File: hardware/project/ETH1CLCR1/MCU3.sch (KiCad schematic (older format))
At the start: 19 parts, among them J601 Conn_02x05, U601 STM32F413RGT6Tx, U602 24LC08B-E/MS, Y601 NX3225GD-8MHZ-STD-CRA-3

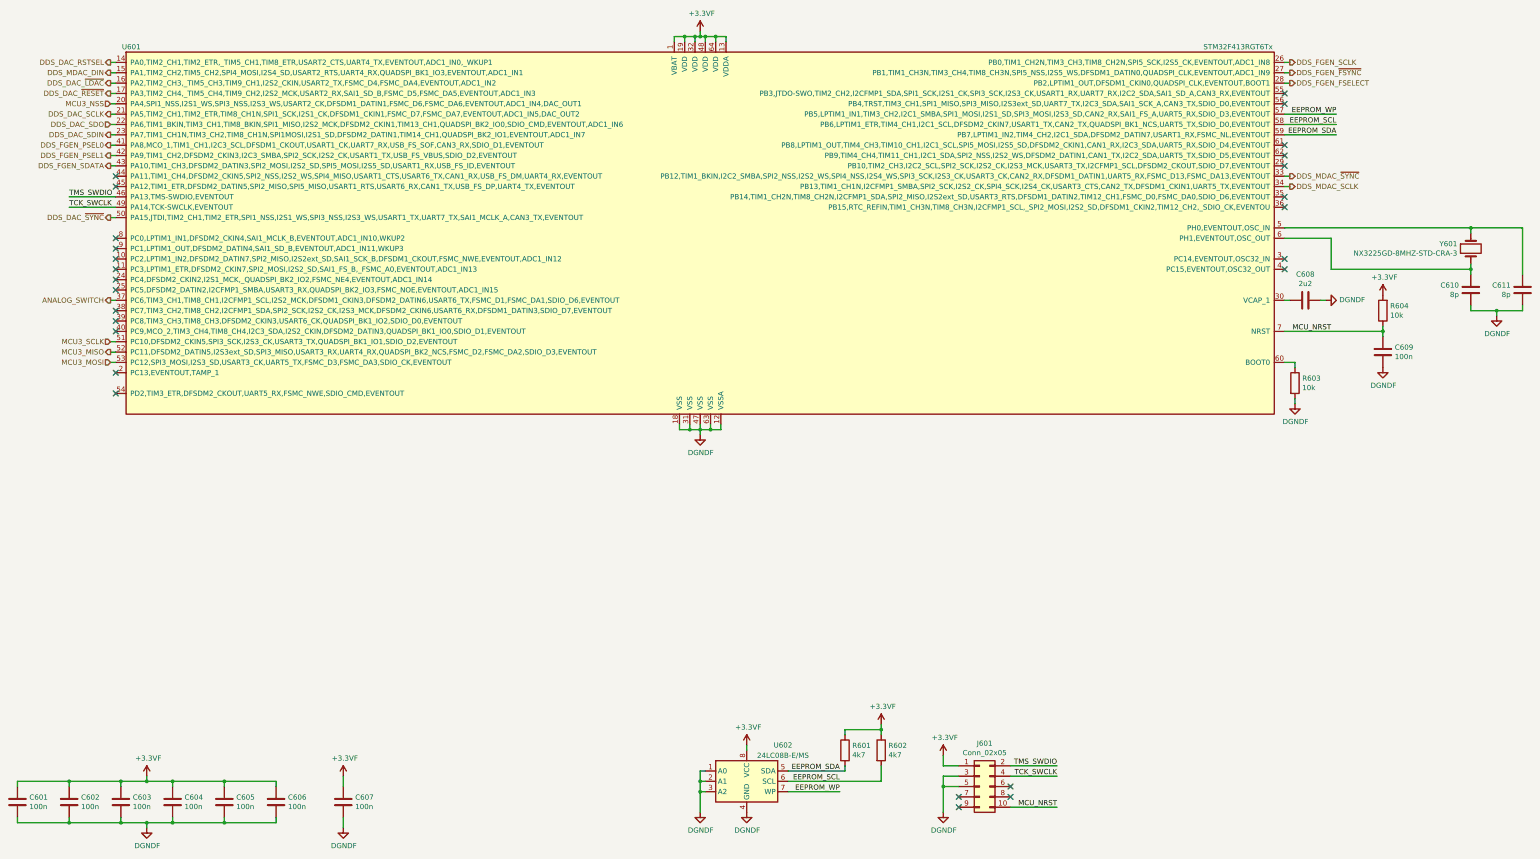
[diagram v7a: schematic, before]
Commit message: Checked the schematics. Created BOM.
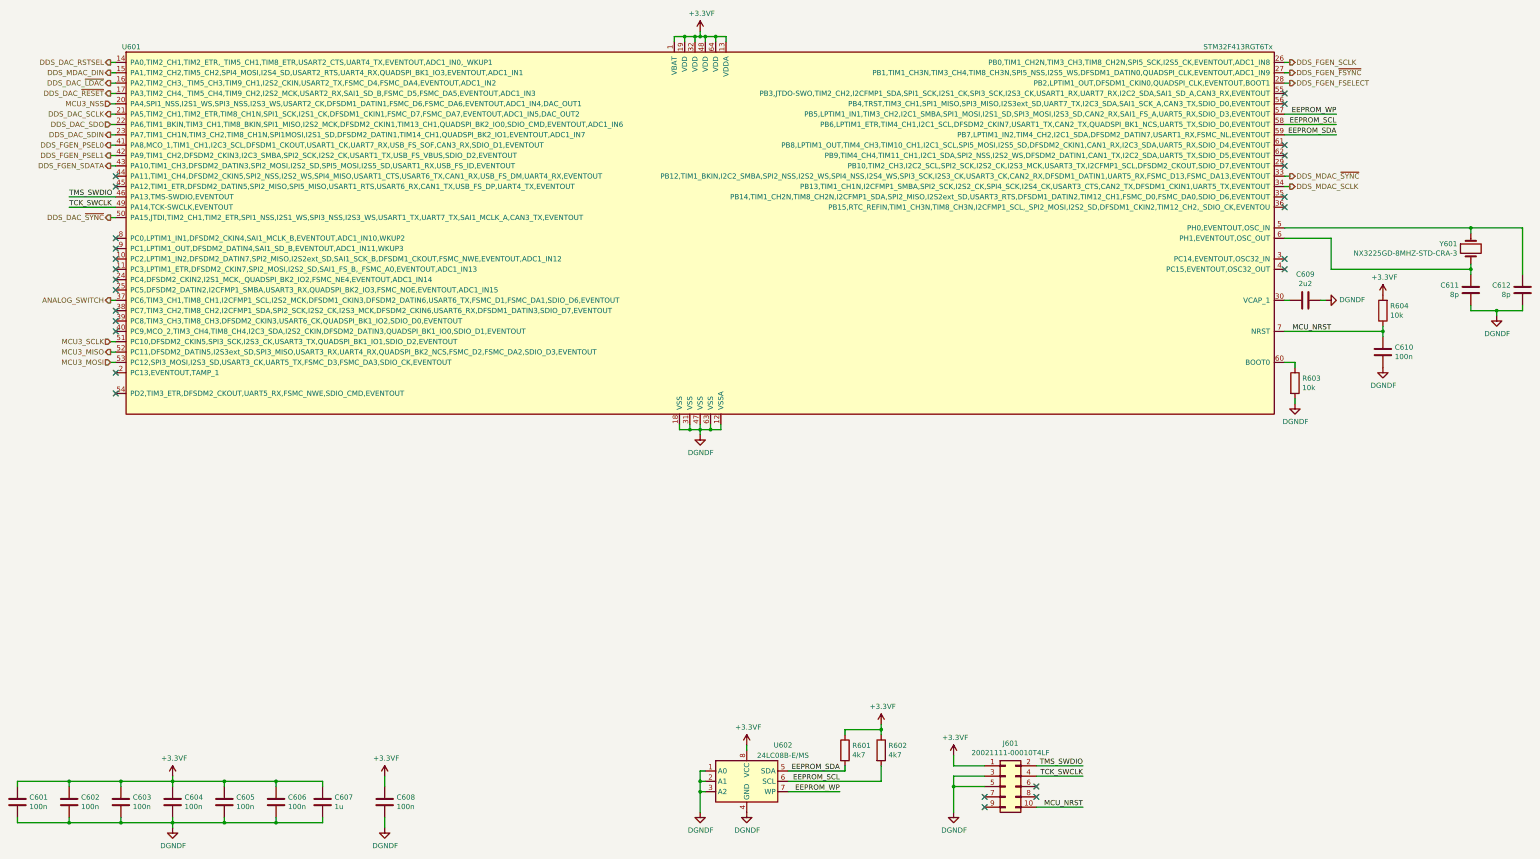
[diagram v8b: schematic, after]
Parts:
- added C607: 1u, Capacitor_SMD:C_0603_1608Metric_Pad1.05x0.95mm_HandSolder, symbol Device:C
- J601: value Conn_02x05 -> 20021111-00010T4LF
- renumbered C607 to C608, C608 to C609, C609 to C610, C610 to C611, C611 to C612
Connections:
- net +3.3VF: now also C607.1
- net DGNDF: now also C607.2
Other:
- moved on the sheet: C608, J601
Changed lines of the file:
@@
 encoding utf-8
 Sheet 6 15
-Title ""
-Date ""
-Rev ""
+Title "MCU3"
+Date "2020-01-19"
+Rev "1.0"
 Comp ""
-Comment1 ""
+Comment1 "Verification done."
 Comment2 ""
 Comment3 ""
@@
 L Connector_Generic:Conn_02x05_Odd_Even J?
 U 1 1 5E74C1A0
-P 10250 10350
+P 10500 10350
 AR Path="/5DCED281/5E74C1A0" Ref="J?"  Part="1"
 AR Path="/5DF35BC8/5E74C1A0" Ref="J?"  Part="1"
 AR Path="/5E29C232/5E74C1A0" Ref="J?"  Part="1"
 AR Path="/5DF38F82/5E74C1A0" Ref="J601"  Part="1"
-F 0 "J601" H 10300 10767 50  0000 C CNN
-F 1 "Conn_02x05" H 10300 10676 50  0000 C CNN
-F 2 "Connector_PinHeader_1.27mm:PinHeader_2x05_P1.27mm_Vertical" H 10250 10350 50  0001 C CNN
-F 3 "~" H 10250 10350 50  0001 C CNN
-	1    10250 10350
-	1    0    0    -1
-$EndComp
-NoConn ~ 10050 10450
-NoConn ~ 10050 10550
-Wire Wire Line
-	10050 10350 9900 10350
-Wire Wire Line
-	9900 10350 9900 10250
-Wire Wire Line
-	9900 10250 10050 10250
-Wire Wire Line
-	9900 10600 9900 10350
-Connection ~ 9900 10350
-Wire Wire Line
-	9900 10050 9900 10150
-Wire Wire Line
-	9900 10150 10050 10150
-Wire Wire Line
-	10550 10150 11000 10150
-Text Label 11000 10150 2    50   ~ 0
+F 0 "J601" H 10550 10767 50  0000 C CNN
+F 1 "20021111-00010T4LF" H 10550 10676 50  0000 C CNN
+F 2 "Connector_PinHeader_1.27mm:PinHeader_2x05_P1.27mm_Vertical" H 10500 10350 50  0001 C CNN
+F 3 "~" H 10500 10350 50  0001 C CNN
+	1    10500 10350
+	1    0    0    -1
+$EndComp
+NoConn ~ 10300 10450
+NoConn ~ 10300 10550
+Wire Wire Line
+	10300 10350 10000 10350
+Wire Wire Line
+	10000 10350 10000 10250
+Wire Wire Line
+	10000 10250 10300 10250
+Wire Wire Line
+	10000 10600 10000 10350
+Connection ~ 10000 10350
+Wire Wire Line
+	10000 10050 10000 10150
+Wire Wire Line
+	10000 10150 10300 10150
+Wire Wire Line
+	10800 10150 11250 10150
+Text Label 11250 10150 2    50   ~ 0
 TMS_SWDIO
 Wire Wire Line
-	10550 10250 11000 10250
-Text Label 11000 10250 2    50   ~ 0
+	10800 10250 11250 10250
+Text Label 11250 10250 2    50   ~ 0
 TCK_SWCLK
 Wire Wire Line
-	10550 10550 11000 10550
-Text Label 11000 10550 2    50   ~ 0
+	10800 10550 11250 10550
+Text Label 11250 10550 2    50   ~ 0
 MCU_NRST
 $Comp
 L ETH1CLCR1:DGNDF #PWR?
 U 1 1 5E74C1B5
-P 9900 10600
+P 10000 10600
 AR Path="/5DF35BC8/5E74C1B5" Ref="#PWR?"  Part="1"
 AR Path="/5E29C232/5E74C1B5" Ref="#PWR?"  Part="1"
 AR Path="/5DF38F82/5E74C1B5" Ref="#PWR0612"  Part="1"
-F 0 "#PWR0612" H 9900 10350 50  0001 C CNN
-F 1 "DGNDF" H 9905 10427 50  0000 C CNN
-F 2 "" H 9900 10600 50  0001 C CNN
-F 3 "" H 9900 10600 50  0001 C CNN
-	1    9900 10600
-	1    0    0    -1
-$EndComp
-NoConn ~ 10550 10350
-NoConn ~ 10550 10450
+F 0 "#PWR0612" H 10000 10350 50  0001 C CNN
+F 1 "DGNDF" H 10005 10427 50  0000 C CNN
+F 2 "" H 10000 10600 50  0001 C CNN
+F 3 "" H 10000 10600 50  0001 C CNN
+	1    10000 10600
+	1    0    0    -1
+$EndComp
+NoConn ~ 10800 10350
+NoConn ~ 10800 10450
 $Comp
 L Device:Crystal Y?
@@
 AR Path="/5DCED281/5E7594BE" Ref="C?"  Part="1"
 AR Path="/5E29C232/5E7594BE" Ref="C?"  Part="1"
-AR Path="/5DF38F82/5E7594BE" Ref="C610"  Part="1"
-F 0 "C610" H 15115 5596 50  0000 L CNN
+AR Path="/5DF38F82/5E7594BE" Ref="C611"  Part="1"
+F 0 "C611" H 15115 5596 50  0000 L CNN
 F 1 "8p" H 15115 5505 50  0000 L CNN
 F 2 "Capacitor_SMD:C_0603_1608Metric_Pad1.05x0.95mm_HandSolder" H 15038 5400 50  0001 C CNN
@@
 AR Path="/5DCED281/5E7594C4" Ref="C?"  Part="1"
 AR Path="/5E29C232/5E7594C4" Ref="C?"  Part="1"
-AR Path="/5DF38F82/5E7594C4" Ref="C611"  Part="1"
-F 0 "C611" H 15615 5596 50  0000 L CNN
+AR Path="/5DF38F82/5E7594C4" Ref="C612"  Part="1"
+F 0 "C612" H 15615 5596 50  0000 L CNN
 F 1 "8p" H 15615 5505 50  0000 L CNN
 F 2 "Capacitor_SMD:C_0603_1608Metric_Pad1.05x0.95mm_HandSolder" H 15538 5400 50  0001 C CNN
@@
 	8000 9950 8000 10000
 $Comp
-L Device:C C608
+L Device:C C609
 U 1 1 5E776A2B
 P 13400 5650
-F 0 "C608" V 13148 5650 50  0000 C CNN
+F 0 "C609" V 13148 5650 50  0000 C CNN
 F 1 "2u2" V 13239 5650 50  0000 C CNN
 F 2 "Capacitor_SMD:C_0805_2012Metric_Pad1.15x1.40mm_HandSolder" H 13438 5500 50  0001 C CNN
@@
 	13650 5050 13650 5350
 $Comp
-L Device:C C609
+L Device:C C610
 U 1 1 5E7B49DC
 P 14150 6150
-F 0 "C609" H 14265 6196 50  0000 L CNN
+F 0 "C610" H 14265 6196 50  0000 L CNN
 F 1 "100n" H 14265 6105 50  0000 L CNN
 F 2 "Capacitor_SMD:C_0603_1608Metric_Pad1.05x0.95mm_HandSolder" H 14188 6000 50  0001 C CNN
@@
 Connection ~ 1950 10300
 Wire Wire Line
-	1950 10300 2200 10300
-Wire Wire Line
 	1450 10350 1450 10300
 Connection ~ 1450 10300
@@
 Connection ~ 1950 10700
 Wire Wire Line
-	1950 10700 2200 10700
-Wire Wire Line
 	1450 10650 1450 10700
 Connection ~ 1450 10700
@@
 L ETH1CLCR1:DGNDF #PWR0602
 U 1 1 5E107792
-P 2200 10750
-F 0 "#PWR0602" H 2200 10500 50  0001 C CNN
-F 1 "DGNDF" H 2205 10577 50  0000 C CNN
-F 2 "" H 2200 10750 50  0001 C CNN
-F 3 "" H 2200 10750 50  0001 C CNN
-	1    2200 10750
-	1    0    0    -1
-$EndComp
-Wire Wire Line
-	2200 10750 2200 10700
-Connection ~ 2200 10700
-Wire Wire Line
-	2200 10700 2450 10700
-Wire Wire Line
-	2200 10250 2200 10300
-Connection ~ 2200 10300
-Wire Wire Line
-	2200 10300 2450 10300
-$Comp
-L Device:C C607
+P 2450 10750
+F 0 "#PWR0602" H 2450 10500 50  0001 C CNN
+F 1 "DGNDF" H 2455 10577 50  0000 C CNN
+F 2 "" H 2450 10750 50  0001 C CNN
+F 3 "" H 2450 10750 50  0001 C CNN
+	1    2450 10750
+	1    0    0    -1
+$EndComp
+Wire Wire Line
+	2450 10750 2450 10700
+Wire Wire Line
+	2450 10250 2450 10300
+$Comp
+L Device:C C608
 U 1 1 5DEC46E0
-P 4100 10500
-F 0 "C607" H 4215 10546 50  0000 L CNN
-F 1 "100n" H 4215 10455 50  0000 L CNN
-F 2 "Capacitor_SMD:C_0603_1608Metric_Pad1.05x0.95mm_HandSolder" H 4138 10350 50  0001 C CNN
-F 3 "~" H 4100 10500 50  0001 C CNN
-	1    4100 10500
+P 4500 10500
+F 0 "C608" H 4615 10546 50  0000 L CNN
+F 1 "100n" H 4615 10455 50  0000 L CNN
+F 2 "Capacitor_SMD:C_0603_1608Metric_Pad1.05x0.95mm_HandSolder" H 4538 10350 50  0001 C CNN
+F 3 "~" H 4500 10500 50  0001 C CNN
+	1    4500 10500
 	1    0    0    -1
 $EndComp
@@
 L ETH1CLCR1:DGNDF #PWR0604
 U 1 1 5DEC5F6E
-P 4100 10750
-F 0 "#PWR0604" H 4100 10500 50  0001 C CNN
-F 1 "DGNDF" H 4105 10577 50  0000 C CNN
-F 2 "" H 4100 10750 50  0001 C CNN
-F 3 "" H 4100 10750 50  0001 C CNN
-	1    4100 10750
-	1    0    0    -1
-$EndComp
-Wire Wire Line
-	4100 10750 4100 10650
-Wire Wire Line
-	4100 10250 4100 10350
+P 4500 10750
+F 0 "#PWR0604" H 4500 10500 50  0001 C CNN
+F 1 "DGNDF" H 4505 10577 50  0000 C CNN
+F 2 "" H 4500 10750 50  0001 C CNN
+F 3 "" H 4500 10750 50  0001 C CNN
+	1    4500 10750
+	1    0    0    -1
+$EndComp
+Wire Wire Line
+	4500 10750 4500 10650
+Wire Wire Line
+	4500 10250 4500 10350
 Text HLabel 1850 5650 0    50   Output ~ 0
 ANALOG_SWITCH
@@
 L ETH1CLCR1:+3.3VF #PWR0601
 U 1 1 5E94700D
-P 2200 10250
-F 0 "#PWR0601" H 2200 10100 50  0001 C CNN
-F 1 "+3.3VF" H 2215 10423 50  0000 C CNN
-F 2 "" H 2200 10250 50  0001 C CNN
-F 3 "" H 2200 10250 50  0001 C CNN
-	1    2200 10250
+P 2450 10250
+F 0 "#PWR0601" H 2450 10100 50  0001 C CNN
+F 1 "+3.3VF" H 2465 10423 50  0000 C CNN
+F 2 "" H 2450 10250 50  0001 C CNN
+F 3 "" H 2450 10250 50  0001 C CNN
+	1    2450 10250
 	1    0    0    -1
 $EndComp
@@
 L ETH1CLCR1:+3.3VF #PWR0603
 U 1 1 5E9476B2
-P 4100 10250
-F 0 "#PWR0603" H 4100 10100 50  0001 C CNN
-F 1 "+3.3VF" H 4115 10423 50  0000 C CNN
-F 2 "" H 4100 10250 50  0001 C CNN
-F 3 "" H 4100 10250 50  0001 C CNN
-	1    4100 10250
+P 4500 10250
+F 0 "#PWR0603" H 4500 10100 50  0001 C CNN
+F 1 "+3.3VF" H 4515 10423 50  0000 C CNN
+F 2 "" H 4500 10250 50  0001 C CNN
+F 3 "" H 4500 10250 50  0001 C CNN
+	1    4500 10250
 	1    0    0    -1
 $EndComp
@@
 L ETH1CLCR1:+3.3VF #PWR0611
 U 1 1 5E9493FF
-P 9900 10050
-F 0 "#PWR0611" H 9900 9900 50  0001 C CNN
-F 1 "+3.3VF" H 9915 10223 50  0000 C CNN
-F 2 "" H 9900 10050 50  0001 C CNN
-F 3 "" H 9900 10050 50  0001 C CNN
-	1    9900 10050
+P 10000 10050
+F 0 "#PWR0611" H 10000 9900 50  0001 C CNN
+F 1 "+3.3VF" H 10015 10223 50  0000 C CNN
+F 2 "" H 10000 10050 50  0001 C CNN
+F 3 "" H 10000 10050 50  0001 C CNN
+	1    10000 10050
 	1    0    0    -1
 $EndComp
@@
 NoConn ~ 13200 4350
 NoConn ~ 13200 4250
+$Comp
+L Device:C C607
+U 1 1 5E3535F6
+P 3900 10500
+F 0 "C607" H 4015 10546 50  0000 L CNN
+F 1 "1u" H 4015 10455 50  0000 L CNN
+F 2 "Capacitor_SMD:C_0603_1608Metric_Pad1.05x0.95mm_HandSolder" H 3938 10350 50  0001 C CNN
+F 3 "~" H 3900 10500 50  0001 C CNN
+	1    3900 10500
+	1    0    0    -1
+$EndComp
+Wire Wire Line
+	3900 10650 3900 10700
+Wire Wire Line
+	3900 10700 3450 10700
+Connection ~ 3450 10700
+Wire Wire Line
+	3450 10300 3900 10300
+Wire Wire Line
+	3900 10300 3900 10350
+Connection ~ 3450 10300
+Wire Wire Line
+	1950 10300 2450 10300
+Wire Wire Line
+	1950 10700 2450 10700
 $EndSCHEMATC
